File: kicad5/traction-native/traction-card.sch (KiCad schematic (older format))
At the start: 297 parts, among them Y1 CX3225GA40000D0PTVCC

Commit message: Rev A.16: round 17 — gap closure (F174-F189) + round 16 rev A.15 (F167-F173): every gap closed, upgraded or numbered
Round 16 (rev A.15, three rechecks of 32214be): exciter MFB gain 24 k -> 28 k with the amplitude
planes (setpoint 7.2 V pp at the monitor), unidirectional exciter TVS, /33X hold 0.07 A, firmware
acquisition contracts (phase triplets, resolver frame age, coherent SDADC frames); BOM furnished
(spec-class capacitors, drawn-size gate in bom-gen, last placeholders bound with archived sheets).

Round 17 (rev A.16, "close all gaps" / "feel free to upgrade"):
- Hardware: DEXP/DEXN PMEG4050EP-Q rated back-drive diversion (closes the ALM2402 OPEN row);
  exciter TVS -> SMDJ8.5A-HRA (3 kW, AEC-Q101, same pad); fault rows split single fault (PASS
  at any source impedance) vs load-dump-coincident double event; LV entry re-designed as
  LET-THROUGH for ISO 16750-2 test B (TPSMC33A-VR/TPSMC18A-VR anti-series pair at the pin ahead
  of the reverse Schottky, TPSMC33CA-VR on the power board, CLVC3 100 uF hybrid polymer, FLVC
  5 A fuse, DIGN US1M, ULDO15 D2PAK) — pulse 1 was avalanching DREVC, the 2023 26 V jump start
  opened the old TVS, the polyfuse was undersized at 9 V; RFS4 -> ESR18 1206.
- Stale/unsourced rows recomputed: cold-crank excitation, PTC hold (IR-13), discharge resistor
  no-flame statement, hall reference drift, ASC command-path collapse.
- KiCad: a KiCad 9/10 set (kicad/traction, Traction-Inverter-KiCad-modern.zip) proved by
  kicad-cli netlist export on every board with mutation tests; KiCad 10 cannot resolve the KiCad 5
  legacy symbols; the proof exposed harness pins numbered P1-P40 and the SMDJ drawn as a resistor
  in the legacy generator — fixed; sym-lib-table + cache library in both legacy sets.
- Firmware: all 35 open contract items closed (FW-08 zero-current decision, FW-31 liveness,
  FW-32 UDS service-lock routine, FW-33 supply-overvoltage supervision), FS26 watchdog answer
  3.0 ms -> 2.0 ms, ASC-exit release wait CAL, 39-row silicon/RM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
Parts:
- added RCPD1, RCPD2, RCPD3, RHWP: 10k, R0603, symbol traction-r1:R
- CAND1: renamed from CCLR; value 15nF -> 100nF; MPN MLCC-15nF-50V-C0G -> MLCC-CLASS
- CAND2: renamed from CFLTD; value 3.3nF -> 100nF; MPN MLCC-3.3nF-50V-C0G -> MLCC-CLASS
- CASCG: renamed from DFO; value BAT46ZFILM -> 100nF; footprint SOD123 -> C0603; symbol traction-r1:D -> traction-r1:C; LCSC C283255 -> CLASS; MPN BAT46ZFILM -> MLCC-100nF-16V
- CBAL: renamed from CBTP; value 22nF -> 1nF; MPN MLCC-CLASS -> MLCC-1nF-50V-C0G
- CBTC: renamed from CSB1; value 22uF -> 47nF; footprint C0805 -> C0603; MPN MLCC-CLASS -> MLCC-47nF-50V-X7R-0603
- CBTP: renamed from CSB2; value 22uF -> 22nF; footprint C0805 -> C0603; MPN MLCC-CLASS -> MLCC-22nF-50V-X7R-0603
- CCAN1: renamed from LCAN2; value ACT45B-101-2P-TL003 -> 1uF; footprint CMC1210 -> C0603; symbol traction-r1:ACT45B-101-2P-TL003 -> traction-r1:C; MPN ACT45B-101-2P-TL003 -> MLCC-1uF-25V
- CCAN2: renamed from JVEH; value TE 770669-1 (AMPSEAL 23) -> 1uF; footprint AMPSEAL23 -> C0603; symbol traction-r1:TE_770669-1__AMPSEAL_23_ -> traction-r1:C; MPN TE 770669-1 (AMPSEAL 23) -> MLCC-1uF-25V
- CCLR: renamed from CFLTF; value 100pF -> 15nF; MPN MLCC-100pF-16V -> MLCC-15nF-50V-C0G
- CCOSA1: renamed from CCOSF1; MPN MLCC-CLASS -> MLCC-22pF-50V-C0G-0603
- CCOSA2: renamed from CCOSF2; value 22pF -> 220pF; MPN MLCC-CLASS -> MLCC-220pF-50V-C0G-0603
- CCOSA3: renamed from RCOS1; value 12k -> 22pF; footprint R0603 -> C0603; symbol traction-r1:R -> traction-r1:C; MPN R0603-CLASS -> MLCC-22pF-50V-C0G-0603
- CCOSD: renamed from RCOS2; value 12k -> 47pF; footprint R0603 -> C0603; symbol traction-r1:R -> traction-r1:C; MPN R0603-CLASS -> MLCC-47pF-50V-C0G-0603
- CCOSF1: renamed from RCOSF1; value 12k -> 22pF; footprint R0603 -> C0603; symbol traction-r1:R -> traction-r1:C; MPN R0603-CLASS -> MLCC-22pF-50V-C0G-0603
- CCOSF2: renamed from RCOSF2; value 12k -> 22pF; footprint R0603 -> C0603; symbol traction-r1:R -> traction-r1:C; MPN R0603-CLASS -> MLCC-22pF-50V-C0G-0603
- CCT1: renamed from TVSC2; value PESD2IVN24-T -> 4.7nF; footprint SOT23 -> C0603; symbol traction-r1:PESD2IVN24-T -> traction-r1:C; LCSC C406047 -> CLASS; MPN PESD2IVN24-T -> MLCC-4.7nF-50V
- CCT2: renamed from FVS1; value MF-LSMF -> 4.7nF; footprint PTC1206 -> C0603; symbol traction-r1:F -> traction-r1:C; MPN MF-LSMF-CLASS -> MLCC-4.7nF-50V
- CEXA1: renamed from CEXA3; value 100nF -> 220pF; MPN MLCC-CLASS -> MLCC-220pF-50V-C0G-0603
- CEXA2: renamed from CEXA4; value 47pF -> 1.5nF; MPN MLCC-CLASS -> MLCC-1.5nF-50V-C0G-0603
- CEXA3: renamed from CEXD; value 4.7uF -> 100nF; MPN MLCC-CLASS -> MLCC-100nF-50V-X7R-0603
- CEXA4: renamed from CEXM; value 220pF -> 47pF; MPN MLCC-220pF-50V-C0G -> MLCC-47pF-50V-C0G-0603
- CEXD: renamed from CLDE; value 22uF -> 4.7uF; footprint C0603 -> C1206; MPN MLCC-CLASS -> MLCC-4.7uF-25V-X7R
- CEXM: renamed from CLDEC; value 270pF -> 220pF; MPN MLCC-CLASS -> MLCC-220pF-50V-C0G
- CFLTD: renamed from CFLTF2; value 100pF -> 3.3nF; MPN MLCC-100pF-16V -> MLCC-3.3nF-50V-C0G
- CFLTF: renamed from CLAT2; value 100nF -> 100pF; MPN MLCC-100nF-16V -> MLCC-100pF-16V
- CFLTF2: renamed from CSCH; value 100nF -> 100pF; MPN MLCC-100nF-16V -> MLCC-100pF-16V
- CIGN: renamed from DIGN; value 1N4148WS -> 100nF; footprint SOD323 -> C0603; symbol traction-r1:D -> traction-r1:C; LCSC C2128 -> CLASS; MPN 1N4148WS -> MLCC-100nF-50V
- CIGNS: renamed from RIGN1; value 5.1k -> 100nF; footprint R0603 -> C0603; symbol traction-r1:R -> traction-r1:C; MPN R0603-5k1 -> MLCC-CLASS
- CILK: renamed from RILK2; value 10k -> 2.2nF; footprint R0603 -> C0603; symbol traction-r1:R -> traction-r1:C; MPN R0603-10k -> MLCC-2.2nF-50V
- CLAT: renamed from RARB; value 10k -> 100nF; footprint R0603 -> C0603; symbol traction-r1:R -> traction-r1:C; MPN R0603-10k -> MLCC-100nF-16V
- CLDE: renamed from FEXN; value MF-MSMF020/33X -> 22uF; footprint 1812 -> C1210; symbol traction-r1:F -> traction-r1:C; MPN MF-MSMF020/33X -> MLCC-22uF-25V-X7R-1210
- CLDEC: renamed from FEXP; value MF-MSMF020/33X -> 270pF; footprint 1812 -> C0603; symbol traction-r1:F -> traction-r1:C; MPN MF-MSMF020/33X -> MLCC-270pF-50V-C0G-0603
- CLVC3: renamed from CLVSM; value 100nF -> 100uF; footprint C0603 -> CAP-ALU-SMD-G-10x10.2; symbol traction-r1:C -> traction-r1:CP; MPN MLCC-100nF-50V -> EEH-ZC1H101P
- CLVSM: renamed from DREVC; value STPS5L60S -> 100nF; footprint SMC -> C0603; symbol traction-r1:D -> traction-r1:C; LCSC C140620 -> CLASS; MPN STPS5L60S -> MLCC-100nF-50V
- CMD1, CMD10, CMD11, CMD12, CMD2, CMD3, CMD4, CMD5, CMD6, CMD7, CMD8, CMD9: footprint C0402 -> C0603; MPN MLCC-100nF-16V -> MLCC-100nF-16V-X7R-0603
- CMT1F: renamed from RMT1P; value 10k -> 47nF; footprint R0603 -> C0603; symbol traction-r1:R -> traction-r1:C; MPN R0603-CLASS -> MLCC-47nF-25V
- CMT2F: renamed from RMT1S; value 1k -> 47nF; footprint R0603 -> C0603; symbol traction-r1:R -> traction-r1:C; MPN R0603-CLASS -> MLCC-47nF-25V
- COF1: renamed from RVD1A; value 10k -> 100nF; footprint R0603 -> C0603; symbol traction-r1:R -> traction-r1:C; MPN R0603-10k-0.1% -> MLCC-CLASS
- COR1: renamed from CILK; value 2.2nF -> 100nF; MPN MLCC-2.2nF-50V -> MLCC-CLASS
- COR2: renamed from RILK1; value 10k -> 100nF; footprint R0603 -> C0603; symbol traction-r1:R -> traction-r1:C; MPN R0603-10k -> MLCC-CLASS
- CSB1: renamed from CSB3; MPN MLCC-CLASS -> MLCC-22uF-16V-X7R-0805
- CSB2: renamed from CSB3B; footprint C0603 -> C0805; MPN MLCC-CLASS -> MLCC-22uF-16V-X7R-0805
- CSB3: renamed from CSB4; value 10uF -> 22uF; MPN MLCC-CLASS -> MLCC-22uF-10V-X7R-0805
- CSB3B: renamed from CSB5; value 1uF -> 22uF; MPN MLCC-1uF-16V-X7R-0805 -> MLCC-22uF-10V-X7R-0805
- CSB4: renamed from CSB6; value 4.7uF -> 10uF; MPN MLCC-CLASS -> MLCC-10uF-10V-X7R-0805
- CSB5: renamed from CSB7; value 10uF -> 1uF; MPN MLCC-CLASS -> MLCC-1uF-16V-X7R-0805
- CSB6: renamed from CSB8; value 10uF -> 4.7uF; MPN MLCC-CLASS -> MLCC-4.7uF-10V-X7R-0805
- CSB7: renamed from CVBOS; value 4.7uF -> 10uF; footprint C0603 -> C0805; MPN MLCC-CLASS -> MLCC-10uF-16V-X7R-0805
- CSB8: renamed from CVDIG; value 1uF -> 10uF; footprint C0603 -> C0805; MPN MLCC-CLASS -> MLCC-10uF-16V-X7R-0805
- CSCH2: renamed from DCLR; value BAT46ZFILM -> 100nF; footprint SOD123 -> C0603; symbol traction-r1:D -> traction-r1:C; LCSC C283255 -> CLASS; MPN BAT46ZFILM -> MLCC-100nF-16V
- CSCH3: renamed from DFLT1; value BAT46ZFILM -> 100nF; footprint SOD123 -> C0603; symbol traction-r1:D -> traction-r1:C; LCSC C283255 -> CLASS; MPN BAT46ZFILM -> MLCC-100nF-16V
- CSINA1: renamed from CSINF1; MPN MLCC-CLASS -> MLCC-22pF-50V-C0G-0603
- CSINA2: renamed from CSINF2; value 22pF -> 220pF; MPN MLCC-CLASS -> MLCC-220pF-50V-C0G-0603
- CSINA3: renamed from RSIN1; value 12k -> 22pF; footprint R0603 -> C0603; symbol traction-r1:R -> traction-r1:C; MPN R0603-CLASS -> MLCC-22pF-50V-C0G-0603
- CSIND: renamed from RSIN2; value 12k -> 47pF; footprint R0603 -> C0603; symbol traction-r1:R -> traction-r1:C; MPN R0603-CLASS -> MLCC-47pF-50V-C0G-0603
- CSINF1: renamed from RSINF1; value 12k -> 22pF; footprint R0603 -> C0603; symbol traction-r1:R -> traction-r1:C; MPN R0603-CLASS -> MLCC-22pF-50V-C0G-0603
- CSINF2: renamed from RSINF2; value 12k -> 22pF; footprint R0603 -> C0603; symbol traction-r1:R -> traction-r1:C; MPN R0603-CLASS -> MLCC-22pF-50V-C0G-0603
- CSNUF: renamed from RSNVP; value 5.1k -> 47nF; footprint R0603 -> C0603; symbol traction-r1:R -> traction-r1:C; MPN R0603-5k1-1% -> MLCC-47nF-25V
- CSNVF: renamed from RSNWP; value 5.1k -> 47nF; footprint R0603 -> C0603; symbol traction-r1:R -> traction-r1:C; MPN R0603-5k1-1% -> MLCC-47nF-25V
- CSNWF: renamed from RTMR; value 0R -> 47nF; footprint R0603 -> C0603; symbol traction-r1:R -> traction-r1:C; MPN R0603-CLASS -> MLCC-47nF-25V
- CTAMBF: renamed from RTHS; value 10k -> 47nF; footprint R0603 -> C0603; symbol traction-r1:R -> traction-r1:C; MPN NTC-10k-0603 -> MLCC-47nF-25V
- CTHSF: renamed from RTHSP; value 10k -> 47nF; footprint R0603 -> C0603; symbol traction-r1:R -> traction-r1:C; MPN R0603-10k-1% -> MLCC-47nF-25V
- CUB1: renamed from LUB; value FB-220R-1A -> 3.3nF; footprint FB0805 -> C0603; symbol traction-r1:L -> traction-r1:C; MPN FB-220R-1A -> MLCC-3.3nF-50V
- CUB2: renamed from RUB0; value 100k -> 100nF; footprint R0603 -> C0603; symbol traction-r1:R -> traction-r1:C; MPN R0603-100k -> MLCC-100nF-25V
- CUS1: renamed from RUB1; value 100R -> 47nF; footprint R0603 -> C0603; symbol traction-r1:R -> traction-r1:C; MPN R0603-100R -> MLCC-47nF-25V
- CUS2: renamed from RUB2; value 100R -> 4.7nF; footprint R0603 -> C0603; symbol traction-r1:R -> traction-r1:C; MPN R0603-100R -> MLCC-4.7nF-50V
- CVB1: renamed from LVB; value FB-220R-1A -> 3.3nF; footprint FB0805 -> C0603; symbol traction-r1:L -> traction-r1:C; MPN FB-220R-1A -> MLCC-3.3nF-50V
- CVB2: renamed from RVB0; value 100k -> 100nF; footprint R0603 -> C0603; symbol traction-r1:R -> traction-r1:C; MPN R0603-100k -> MLCC-100nF-25V
- CVBOS: renamed from DBAT; value BAT46ZFILM -> 4.7uF; footprint SOD123 -> C0805; symbol traction-r1:D -> traction-r1:C; LCSC C283255 -> CLASS; MPN BAT46ZFILM -> MLCC-4.7uF-25V-X7R-0805
- CVD1: renamed from RVD1B; value 10k -> 100pF; footprint R0603 -> C0603; symbol traction-r1:R -> traction-r1:C; MPN R0603-10k-0.1% -> MLCC-100pF-50V-C0G-0603
- CVD2: renamed from RVD2D; value 10k -> 100pF; footprint R0603 -> C0603; symbol traction-r1:R -> traction-r1:C; MPN R0603-10k-0.1% -> MLCC-100pF-50V-C0G-0603
- CVDIG: renamed from LCOR; value XAL4020-222MEC -> 1uF; footprint XAL4020 -> C0603; symbol traction-r1:L -> traction-r1:C; MPN XAL4020-222MEC -> MLCC-1uF-10V-X7R-0603
- CVM1: renamed from RVM1; value 24k -> 220nF; footprint R0603 -> C0603; symbol traction-r1:R -> traction-r1:C; MPN R0603-24k-1% -> MLCC-220nF-16V-X7R-0603
- CVM2: renamed from RVM2; value 24k -> 220nF; footprint R0603 -> C0603; symbol traction-r1:R -> traction-r1:C; MPN R0603-24k-1% -> MLCC-220nF-16V-X7R-0603
- CVS1: renamed from RVB1; value 100R -> 47nF; footprint R0603 -> C0603; symbol traction-r1:R -> traction-r1:C; MPN R0603-100R -> MLCC-47nF-25V
- CVS2: renamed from RVB2; value 100R -> 4.7nF; footprint R0603 -> C0603; symbol traction-r1:R -> traction-r1:C; MPN R0603-100R -> MLCC-4.7nF-50V
- CWB1: renamed from LWB; value FB-220R-1A -> 3.3nF; footprint FB0805 -> C0603; symbol traction-r1:L -> traction-r1:C; MPN FB-220R-1A -> MLCC-3.3nF-50V
- CWB2: renamed from RWB0; value 100k -> 100nF; footprint R0603 -> C0603; symbol traction-r1:R -> traction-r1:C; MPN R0603-100k -> MLCC-100nF-25V
- CWS1: renamed from RWB1; value 100R -> 47nF; footprint R0603 -> C0603; symbol traction-r1:R -> traction-r1:C; MPN R0603-100R -> MLCC-47nF-25V
- CWS2: renamed from RWB2; value 100R -> 4.7nF; footprint R0603 -> C0603; symbol traction-r1:R -> traction-r1:C; MPN R0603-100R -> MLCC-4.7nF-50V
- DBAT: renamed from LSBC; value XAL4040-103MEC -> BAT46ZFILM; footprint XAL4040 -> SOD123; symbol traction-r1:L -> traction-r1:D; LCSC CLASS -> C283255; MPN XAL4040-103MEC -> BAT46ZFILM
- DCOSP: renamed from CCOSD; value 47pF -> PESD2IVN24-T; footprint C0603 -> SOT23; symbol traction-r1:C -> traction-r1:PESD2IVN24-T; LCSC CLASS -> C406047; MPN MLCC-CLASS -> PESD2IVN24-T
- DEXN: renamed from REXA1; value 3k -> PMEG4050EP-Q; footprint R0603 -> SOD128; symbol traction-r1:R -> traction-r1:D; MPN R0603-CLASS -> PMEG4050EP-Q
- DEXP: renamed from REXA2; value 10k -> PMEG4050EP-Q; footprint R0603 -> SOD128; symbol traction-r1:R -> traction-r1:D; MPN R0603-CLASS -> PMEG4050EP-Q
- DFLT1: renamed from RDRB; value 10k -> BAT46ZFILM; footprint R0603 -> SOD123; symbol traction-r1:R -> traction-r1:D; LCSC CLASS -> C283255; MPN R0603-10k -> BAT46ZFILM
- DFLT2: renamed from RENP1; value 5.1k -> BAT46ZFILM; footprint R0603 -> SOD123; symbol traction-r1:R -> traction-r1:D; LCSC CLASS -> C283255; MPN R0603-5k1 -> BAT46ZFILM
- DFO: renamed from RASCP; value 10k -> BAT46ZFILM; footprint R0603 -> SOD123; symbol traction-r1:R -> traction-r1:D; LCSC CLASS -> C283255; MPN R0603-10k -> BAT46ZFILM
- DIGN: renamed from RIGN2; value 10k -> US1M; footprint R0603 -> SMA; symbol traction-r1:R -> traction-r1:D; LCSC CLASS -> C412437; MPN R0603-10k -> US1M
- DREVC: renamed from DTVSC; value TPSMC24CA-VR -> STPS5L60S; LCSC C1975284 -> C140620; MPN TPSMC24CA-VR -> STPS5L60S
- DSINP: renamed from CSIND; value 47pF -> PESD2IVN24-T; footprint C0603 -> SOT23; symbol traction-r1:C -> traction-r1:PESD2IVN24-T; LCSC CLASS -> C406047; MPN MLCC-CLASS -> PESD2IVN24-T
- DTVSC: renamed from FLVC; value MF-LSMF300/24X-2 -> TPSMC33A-VR; footprint PTC2920 -> SMC; symbol traction-r1:F -> traction-r1:D; LCSC C719172 -> CLASS; MPN MF-LSMF300/24X-2 -> TPSMC33A-VR
- DTVSC2: renamed from FVBH; value MF-LSMF300/24X-2 -> TPSMC18A-VR; footprint PTC2920 -> SMC; symbol traction-r1:F -> traction-r1:D; LCSC C719172 -> CLASS; MPN MF-LSMF300/24X-2 -> TPSMC18A-VR
- FEXN: renamed from REXA3; value 10k -> MF-MSMF020/33X; footprint R0603 -> 1812; symbol traction-r1:R -> traction-r1:F; MPN R0603-CLASS -> MF-MSMF020/33X
- FEXP: renamed from REXA4; value 24k -> MF-MSMF020/33X; footprint R0603 -> 1812; symbol traction-r1:R -> traction-r1:F; MPN R0603-CLASS -> MF-MSMF020/33X
- FLVC: renamed from FVBL; value MF-LSMF300/24X-2 -> 0680L5000-05; footprint PTC2920 -> 2410; LCSC C719172 -> CLASS; MPN MF-LSMF300/24X-2 -> 0680L5000-05
- FMT1: renamed from RMT2P; value 10k -> 0438.375WRA; footprint R0603 -> F0603; symbol traction-r1:R -> traction-r1:F; MPN R0603-CLASS -> 0438.375WRA
- FMT2: renamed from RMT2S; value 1k -> 0438.375WRA; footprint R0603 -> F0603; symbol traction-r1:R -> traction-r1:F; MPN R0603-CLASS -> 0438.375WRA
- FVBH: renamed from LFC; value FB-120R-3A -> MF-LSMF300/24X-2; footprint FB1206 -> PTC2920; symbol traction-r1:L -> traction-r1:F; LCSC CLASS -> C719172; MPN FB-120R-3A -> MF-LSMF300/24X-2
- FVBL: renamed from RLVSD; value 4.7k -> MF-LSMF300/24X-2; footprint R0603 -> PTC2920; symbol traction-r1:R -> traction-r1:F; LCSC CLASS -> C719172; MPN R0603-4k7 -> MF-LSMF300/24X-2
- FVS1: renamed from LVS4; value FB-470R -> MF-MSMF010/60X; footprint FB0603 -> PTC1812; symbol traction-r1:L -> traction-r1:F; MPN FB-470R-CLASS -> MF-MSMF010/60X
- JICC: renamed from RCPD3; value 10k -> IPL1-120-01-L-D-K; footprint R0603 -> HDR2x20-2.54; symbol traction-r1:R -> traction-r1:IPL1-120-01-L-D-K; MPN R0603-10k -> IPL1-120-01-L-D-K
- JLEM: renamed from UUB1; value OPA376AQDBVRQ1 -> T2M-105-01-L-D-TH-WT; footprint SOT23-5 -> HDR2x5; symbol traction-r1:OPA376AQDBVRQ1 -> traction-r1:T2M-105-01-L-D-TH-WT; MPN OPA376AQDBVRQ1 -> T2M-105-01-L-D-TH-WT
- JVEH: renamed from LVS3; value FB-470R -> TE 770669-1 (AMPSEAL 23); footprint FB0603 -> AMPSEAL23; symbol traction-r1:L -> traction-r1:TE_770669-1__AMPSEAL_23_; MPN FB-470R-CLASS -> TE 770669-1 (AMPSEAL 23)
- LCAN1: renamed from CCT1; value 4.7nF -> ACT45B-101-2P-TL003; footprint C0603 -> CMC1210; symbol traction-r1:C -> traction-r1:ACT45B-101-2P-TL003; MPN MLCC-4.7nF-50V -> ACT45B-101-2P-TL003
- LCAN2: renamed from CCT2; value 4.7nF -> ACT45B-101-2P-TL003; footprint C0603 -> CMC1210; symbol traction-r1:C -> traction-r1:ACT45B-101-2P-TL003; MPN MLCC-4.7nF-50V -> ACT45B-101-2P-TL003
- LCOR: renamed from RAGT; value 0R -> XAL4020-222MEC; footprint R0603 -> XAL4020; symbol traction-r1:R -> traction-r1:L; MPN R0603-CLASS -> XAL4020-222MEC
- LFC: renamed from RLVSG; value 10k -> BLM31PG121SH1L; footprint R0603 -> FB1206; symbol traction-r1:R -> traction-r1:L; MPN R0603-10k -> BLM31PG121SH1L
- LSBC: renamed from RDBG; value 10k -> XAL4040-103MEC; footprint R0603 -> XAL4040; symbol traction-r1:R -> traction-r1:L; MPN R0603-CLASS -> XAL4040-103MEC
- LUB: renamed from RUB3; value 100R -> BLM21PG221SH1D; footprint R0603 -> FB0805; symbol traction-r1:R -> traction-r1:L; MPN R0603-100R -> BLM21PG221SH1D
- LVB: renamed from RVB3; value 100R -> BLM21PG221SH1D; footprint R0603 -> FB0805; symbol traction-r1:R -> traction-r1:L; MPN R0603-100R -> BLM21PG221SH1D
- LVS1: renamed from JICC; value IPL1-120-01-L-D-K -> MMZ1608B471CTDH5; footprint HDR2x20-2.54 -> FB0603; symbol traction-r1:IPL1-120-01-L-D-K -> traction-r1:L; MPN IPL1-120-01-L-D-K -> MMZ1608B471CTDH5
- LVS2: renamed from RCPD0; value 10k -> MMZ1608B471CTDH5; footprint R0603 -> FB0603; symbol traction-r1:R -> traction-r1:L; MPN R0603-10k -> MMZ1608B471CTDH5
- LVS3: renamed from RCPD1; value 10k -> MMZ1608B471CTDH5; footprint R0603 -> FB0603; symbol traction-r1:R -> traction-r1:L; MPN R0603-10k -> MMZ1608B471CTDH5
- LVS4: renamed from RCPD2; value 10k -> MMZ1608B471CTDH5; footprint R0603 -> FB0603; symbol traction-r1:R -> traction-r1:L; MPN R0603-10k -> MMZ1608B471CTDH5
- LWB: renamed from RWB3; value 100R -> BLM21PG221SH1D; footprint R0603 -> FB0805; symbol traction-r1:R -> traction-r1:L; MPN R0603-100R -> BLM21PG221SH1D
- QBAL: renamed from CBAL; value 1nF -> SQ2310ES; footprint C0603 -> SOT23; symbol traction-r1:C -> traction-r1:SQ2310ES; MPN MLCC-1nF-50V-C0G -> SQ2310ES
- RAGT: renamed from RSB1; value 52.3k -> 0R; footprint R0603 -> R0805; MPN R0603-CLASS -> R0805-0R-CLASS
- RARB: renamed from RFS1; value 1k -> 10k; MPN R0603-1k -> R0603-10k
- RCOS1: renamed from RCOSR1; value 120R -> 12k; MPN R0603-120R -> R0603-CLASS
- RCOS2: renamed from RCOSR2; value 120R -> 12k; MPN R0603-120R -> R0603-CLASS
- RCOSF1: renamed from JLEM; value T2M-105-01-L-D-TH-WT -> 12k; footprint HDR2x5 -> R0603; symbol traction-r1:T2M-105-01-L-D-TH-WT -> traction-r1:R; MPN T2M-105-01-L-D-TH-WT -> R0603-CLASS
- RCOSF2: renamed from USNSU; value HC5FW900-S -> 12k; footprint OffBoard -> R0603; symbol traction-r1:HC5FW900-S -> traction-r1:R; MPN HC5FW900-S -> R0603-CLASS
- RCOSR1: renamed from USNSV; value HC5FW900-S -> 120R; footprint OffBoard -> R0603; symbol traction-r1:HC5FW900-S -> traction-r1:R; MPN HC5FW900-S -> R0603-120R
- RCOSR2: renamed from USNSW; value HC5FW900-S -> 120R; footprint OffBoard -> R0603; symbol traction-r1:HC5FW900-S -> traction-r1:R; MPN HC5FW900-S -> R0603-120R
- RCPD0: renamed from RHWP; MPN R0603-10k-1% -> R0603-10k
- RCT1A: renamed from UCAN2; value TCAN1042HGVDRQ1 -> 60.4R; footprint SOIC8 -> R0603; symbol traction-r1:TCAN1042HGVDRQ1 -> traction-r1:R; LCSC C132550 -> CLASS; MPN TCAN1042HGVDRQ1 -> R0603-60R4-1%
- RCT1B: renamed from CCAN2; value 1uF -> 60.4R; footprint C0603 -> R0603; symbol traction-r1:C -> traction-r1:R; MPN MLCC-1uF-25V -> R0603-60R4-1%
- RCT2A: renamed from LVS1; value FB-470R -> 60.4R; footprint FB0603 -> R0603; symbol traction-r1:L -> traction-r1:R; MPN FB-470R-CLASS -> R0603-60R4-1%
- RCT2B: renamed from LVS2; value FB-470R -> 60.4R; footprint FB0603 -> R0603; symbol traction-r1:L -> traction-r1:R; MPN FB-470R-CLASS -> R0603-60R4-1%
- RDRB: renamed from RFCB; value 100k -> 10k; MPN R0603-100k -> R0603-10k
- RENP1: renamed from RFLTC; value 10k -> 5.1k; MPN R0603-10k -> R0603-5k1
- REXA1: renamed from REXB1; value 24k -> 3k
- REXA2: renamed from REXB2; value 24k -> 10k
- REXA3: renamed from REXB3; value 24k -> 10k
- REXA4: renamed from REXB4; value 24k -> 28k
- REXB1: renamed from REXM1; value 18k -> 24k; MPN R0603-18k-1% -> R0603-CLASS
- REXB2: renamed from REXM2; value 42.2k -> 24k; MPN R0603-42k2-1% -> R0603-CLASS
- REXB3: renamed from REXM3; value 18k -> 24k; MPN R0603-18k-1% -> R0603-CLASS
- REXB4: renamed from REXM4; value 84.5k -> 24k; MPN R0603-84k5-1% -> R0603-CLASS
- REXM1: renamed from RLDE1; value 38.3k -> 18k; MPN R0603-CLASS -> R0603-18k-1%
- REXM2: renamed from RLDE2; value 10k -> 42.2k; MPN R0603-CLASS -> R0603-42k2-1%
- REXM3: renamed from RSDN; value 10k -> 18k; MPN R0603-CLASS -> R0603-18k-1%
- REXM4: renamed from RSXN; value 2.2R -> 84.5k; footprint R1206 -> R0603; MPN R1206-2R2-1% -> R0603-84k5-1%
- RFCB: renamed from RFLTD; value 10k -> 100k; MPN R0603-10k -> R0603-100k
- RFLTC: renamed from RFLTP1; value 5.1k -> 10k; MPN R0603-5k1 -> R0603-10k
- RFLTD: renamed from RFLTP2; value 5.1k -> 10k; MPN R0603-5k1 -> R0603-10k
- RFLTP1: renamed from RGPD; value 10k -> 5.1k; MPN R0603-10k -> R0603-5k1
- RFLTP2: renamed from RLAT2; value 10k -> 5.1k; MPN R0603-10k -> R0603-5k1
- RFS2: renamed from RFS4; value 1k -> 10k; MPN ESR03EZPF1001 -> R0603-10k
- RFS3: renamed from RLAT1; value 10k -> 1k; MPN R0603-10k -> R0603-1k
- RFS4: renamed from ZSET; value BZT52-B5V6 -> 1k; footprint SOD123 -> R1206; symbol traction-r1:D -> traction-r1:R; MPN BZT52-B5V6 -> ESR18EZPF1001
- RIGN1: renamed from RIGNS1; value 47k -> 5.1k; MPN R0603-CLASS -> R0603-5k1
- RIGN2: renamed from RIGNS2; MPN R0603-CLASS -> R0603-10k
- RIGNS1: renamed from UAND1; value 74LVC1G11GW-Q100 -> 47k; footprint SOT363 -> R0603; symbol traction-r1:74LVC1G11GW-Q100 -> traction-r1:R; LCSC C548242 -> CLASS; MPN 74LVC1G11GW-Q100 -> R0603-CLASS
- RIGNS2: renamed from UAND2; value 74LVC1G11GW-Q100 -> 10k; footprint SOT363 -> R0603; symbol traction-r1:74LVC1G11GW-Q100 -> traction-r1:R; LCSC C548242 -> CLASS; MPN 74LVC1G11GW-Q100 -> R0603-CLASS
- RILK3: renamed from UVMB1; value OPA348AQDBVRQ1 -> 10k; footprint SOT23-5 -> R0603; symbol traction-r1:OPA348AQDBVRQ1 -> traction-r1:R; LCSC C2877787 -> CLASS; MPN OPA348AQDBVRQ1 -> R0603-10k
- RILK4: renamed from UVMB2; value OPA348AQDBVRQ1 -> 10k; footprint SOT23-5 -> R0603; symbol traction-r1:OPA348AQDBVRQ1 -> traction-r1:R; LCSC C2877787 -> CLASS; MPN OPA348AQDBVRQ1 -> R0603-10k
- RLAT1: renamed from UOR1; value 74LVC1G32GW-Q100 -> 10k; footprint SOT353 -> R0603; symbol traction-r1:74LVC1G32GW-Q100 -> traction-r1:R; LCSC C548334 -> CLASS; MPN 74LVC1G32GW-Q100 -> R0603-10k
- RLAT2: renamed from RRDB; value 100k -> 10k; MPN R0603-100k -> R0603-10k
- renumbered CSCH2 to CLAT2, CSCH3 to CSCH, DFLT2 to DCLR, RFS2 to RASCP, RSB2 to RDBG, RFS3 to RFS1, RQDM to RGPD, RILK3 to RILK1, RILK4 to RILK2, RVD2A to RVD1C, RVD2B to RVD1D, RVM3 to RVM1, RVM4 to RVM2, USCH3 to USCH
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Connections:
- net AGND: now also CCOSA1.2, CCOSA3.2, CEXA4.2, CIGNS.2, CLDE.2, CMT1F.2, CMT2F.2, COF1.2, CSINA1.2, CSINA3.2, CSNUF.2, CSNVF.2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; no longer CCAN2.10 (MT1R), CCAN2.12 (MT2R), CEXA3.2, JLEM.2, LCOR.1, LVS1.3 (P3_AGND), RCOSF1.10 (G3), RCOSF1.3 (G1), RCOSF1.6 (G2), RCOSF1.9 (SH), RCOSF2.3, RCOSF2.5 (E1)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
- net AMUXO: now also RSB3.1, USBC.29 (AMUX); no longer RSB1.1, ZLVS.29 (AMUX)
- net ASC_CLR_M: now also RFS3.1; no longer RFS1.1
- net ASC_CLR_N: now also RLAT1.2, ULAT.6 (CLR_N); no longer RFS1.2, RV5GS.6 (CLR_N)
- net ASC_CMD: now also JICC.15 (P15_ASC_CMD), RARB.1, UASCG.4 (Y); no longer CLAT.1, LVS1.15 (P15_ASC_CMD), RV5GP.4 (Y)
- net ASC_CMD_RB: now also RARB.2; no longer CLAT.2
- net ASC_Q: now also RASCP.1, UASCG.2 (A), ULAT.5 (Q); no longer DFO.1, RV5GP.2 (A), RV5GS.5 (Q)
- net ASC_REQ: now also ULAT.1 (CLK), RCPD1.1; no longer LVS3.1, RV5GS.1 (CLK)
- net ASC_SET_B: now also ULAT.7 (PRE_N), USCH2.5 (Y2); no longer RV5GS.7 (PRE_N), ULAT2.5 (Y2)
- net ASC_SET_N: now also RFS1.2, RFS2.2, USCH2.3 (A2), ZSET.2; no longer RARB.2, RASCP.2, RFS4.2, ULAT2.3 (A2)
- net BATSNS: now also DBAT.2, USBC.48 (BATSENSE); no longer CVBOS.2, ZLVS.48 (BATSENSE)
- net BCTRL: now also CBAL.1; no longer RLVSM.1 (G)
- net CAN0_RX: now also UCAN1.4 (RXD); no longer TVSM1.4 (RXD)
- net CAN0_TX: now also UCAN1.1 (TXD); no longer TVSM1.1 (TXD)
- net CAN1_RX: now also UCAN2.4 (RXD); no longer RCT1A.4 (RXD)
- net CAN1_TX: now also UCAN2.1 (TXD); no longer RCT1A.1 (TXD)
- net CANH1: now also LCAN1.4 (A2), LVS1.2, TVSC1.1 (A); no longer RCT2A.2, RMT2P.4 (A2), RMT2S.1 (A)
- net CANH1_T: now also LCAN1.1 (A1), RCT1A.1, UCAN1.7 (CANH); no longer RMT2P.1 (A1), TVSC1.1, TVSM1.7 (CANH)
- net CANH2: now also LCAN2.4 (A2), LVS3.2, TVSC2.1 (A); no longer CCAN1.4 (A2), CCT1.1 (A), JVEH.2
- net CANH2_T: now also LCAN2.1 (A1), RCT2A.1, UCAN2.7 (CANH); no longer CCAN1.1 (A1), RCT1A.7 (CANH), TVSC2.1
- net CANL1: now also LCAN1.3 (B2), LVS2.2, TVSC1.2 (B); no longer RCT2B.2, RMT2P.3 (B2), RMT2S.2 (B)
- net CANL1_T: now also LCAN1.2 (B1), RCT1B.2, UCAN1.6 (CANL); no longer RMT2P.2 (B1), TVSM1.6 (CANL), UCAN1.2
- net CANL2: now also LCAN2.3 (B2), LVS4.2, TVSC2.2 (B); no longer CCAN1.3 (B2), CCT1.2 (B), FVS1.2
- net CANL2_T: now also LCAN2.2 (B1), RCT2B.2, UCAN2.6 (CANL); no longer CCAN1.2 (B1), RCT1A.6 (CANL), UCAN2.2
- net CANS1: now also CCT1.1, RCT1A.2, RCT1B.1; no longer LCAN1.1, TVSC1.2, UCAN1.1
- net CANS2: now also CCT2.1, RCT2A.2, RCT2B.1; no longer LCAN2.1, TVSC2.2, UCAN2.1
- net CORBT: now also CBTC.1, USBC.33 (CORE_BT); no longer USBC.1, ZLVS.33 (CORE_BT)
- net COSF_N: now also CCOSD.2, CCOSF2.1, RCOSF2.2, RCOSR2.1; no longer CCOSA2.1, CCOSF2.2, RCOS2.1, RSINF1.2 (B)
- net COSF_P: now also CCOSD.1, CCOSF1.1, RCOSF1.2, RCOSR1.1; no longer CCOSA1.1, CCOSF1.2, RCOS1.1, RSINF1.1 (A)
- net COS_N: now also CCOSA2.2, CCOSA3.1, RCOSR2.2; no longer RCOS2.2, RSINR1.2, RSINR2.1
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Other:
- note added: "rev A.16 - 26 sections - 301 components"
- note removed: "rev A.14 - 26 sections - 297 components"
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
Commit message: Rev A.17: round 18 — three rechecks of 4425af9 (F190-F198): diversion diodes on the amplifier node (loop passes RSX), diode cell cathode = pin 1 on all 35 diodes, exciter TVS/PTC rows at worst corners + ECU-asleep sustained short (WARN rows, layout rule, QP-RX-04 2b gate), anti-surge RSX, NCV4276C reverse current = QP-RX-05 gate + VR-33, IR-16/IR-42, firmware FW-34..36 (sample freshness, cadence-locked resolver frames, latency sign) + three self-found instances
Co-Authored-By: Claude Fable 5.1 <noreply@anthropic.com>
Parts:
- DBAT, DCLR, DEXN, DEXP, DFLT1, DFLT2, DFO, DIGN, DREVC, DTVSC, DTVSC2, ZLVS, ZSET: symbol traction-r1:D -> traction-r1:D_21
- RSXN, RSXP: MPN ERJ-8ENF2R20V -> ESR18EZPF2R20
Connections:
- net ASC_SET_N: now also ZSET.1; no longer ZSET.2
- net BATSNS: now also DBAT.1; no longer DBAT.2
- net DGND: now also DTVSC2.1, ZSET.2; no longer DTVSC2.2, ZSET.1
- net FAULT_OUT: now also DFO.2; no longer DFO.1
- net FCO: now also DREVC.2, DTVSC.1; no longer DREVC.1, DTVSC.2
- net FLT_CLR_N: now also DCLR.2; no longer DCLR.1
- net FLT_CMB_N: now also DFLT1.2, DFLT2.2; no longer DFLT1.1, DFLT2.1
- net FLT_HS_N: now also DFLT1.1; no longer DFLT1.2
- net FLT_LS_N: now also DFLT2.1; no longer DFLT2.2
- net FOUT_K: now also DFO.1; no longer DFO.2
- net IGN_D: now also DIGN.1; no longer DIGN.2
- net KL15: now also DIGN.2; no longer DIGN.1
- net LVS_G: now also ZLVS.2; no longer ZLVS.1
- net NRC: now also DREVC.1, ZLVS.1; no longer DREVC.2, ZLVS.2
- net TVSM: now also DTVSC.2, DTVSC2.2; no longer DTVSC.1, DTVSC2.1
- net V5A: now also DCLR.1; no longer DCLR.2
- net VBATC: now also DBAT.2; no longer DBAT.1
- net VEXD: now also DEXN.1, DEXP.1; no longer DEXN.2, DEXP.2
- net VREX_N: now also DEXN.2
- net VREX_NX: no longer DEXN.1
- net VREX_P: now also DEXP.2
- net VREX_PX: no longer DEXP.1
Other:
- note added: "rev A.17 - 26 sections - 301 components"
- note removed: "rev A.16 - 26 sections - 301 components"
- moved on the sheet: CEXA1, CEXA2, CEXA3, CEXA4, FEXN, FEXP, REXA1, REXA2, REXA3, REXA4, RSXN, RSXP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

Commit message: Rev A.18: round 19 — three rechecks of e315bf1 (F199-F204): PTC-current row at every permitted voltage (IR-16 0.08/0.14/0.37/0.26 Ω), ≥8 A TVS energy an explicit assumption + QP-RX-04 release criterion, window criterion fixed, exciter TVS → SMDJ7.0A-HRA (coupled island holds the 7.0 V class at a parked 12 V battery / the Marine rail), shared exciter-fault model run for the Marine port (QP-MA-11, kit-loom rule), FW-35 rewritten on an SWG-anchored time origin with clock-derived resync and bounded restart
Co-Authored-By: Claude Fable 5.1 <noreply@anthropic.com>
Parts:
- TVSEN, TVSEP: value SMDJ8.5A-HRA -> SMDJ7.0A-HRA; MPN SMDJ8.5A-HRA -> SMDJ7.0A-HRA
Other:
- note added: "rev A.18 - 26 sections - 301 components"
- note removed: "rev A.17 - 26 sections - 301 components"
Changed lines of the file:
@@
 Title "Traction Inverter — Control Card (S32K396 + FS26, ASIL D)"
 Date "2026-09-23"
-Rev "A.17"
+Rev "A.18"
 Comp "Traction Inverter 220 kW pk - Control card (LV), sheet 4 of 4"
 Comment1 "Inverter = Power board + Cap bank busbar + bolt-on Discharge board (all HV) + Control card (LV); safe state holds with any link lost"
@@
 VEHICLE-IF   -   1 section
 Text Notes 33460 22550 0    60   ~ 0
-rev A.17   -   26 sections   -   301 components
+rev A.18   -   26 sections   -   301 components
 Wire Notes Line
 	33400 23500 37850 23500
@@
 P 33450 7000
 F 0 "TVSEN" H 33450 6840 50  0000 C CNN
-F 1 "SMDJ8.5A-HRA" H 33450 7170 50  0000 C CNN
+F 1 "SMDJ7.0A-HRA" H 33450 7170 50  0000 C CNN
 F 2 "SMC" H 33450 7000 50  0001 C CNN
 F 3 "~" H 33450 7000 50  0001 C CNN
 F 4 "CLASS" H 33450 7000 50  0001 C CNN "LCSC"
-F 5 "SMDJ8.5A-HRA" H 33450 7000 50  0001 C CNN "MPN"
+F 5 "SMDJ7.0A-HRA" H 33450 7000 50  0001 C CNN "MPN"
 	1    33450 7000
 	1    0    0    -1
@@
 P 33450 5800
 F 0 "TVSEP" H 33450 5640 50  0000 C CNN
-F 1 "SMDJ8.5A-HRA" H 33450 5970 50  0000 C CNN
+F 1 "SMDJ7.0A-HRA" H 33450 5970 50  0000 C CNN
 F 2 "SMC" H 33450 5800 50  0001 C CNN
 F 3 "~" H 33450 5800 50  0001 C CNN
 F 4 "CLASS" H 33450 5800 50  0001 C CNN "LCSC"
-F 5 "SMDJ8.5A-HRA" H 33450 5800 50  0001 C CNN "MPN"
+F 5 "SMDJ7.0A-HRA" H 33450 5800 50  0001 C CNN "MPN"
 	1    33450 5800
 	1    0    0    -1

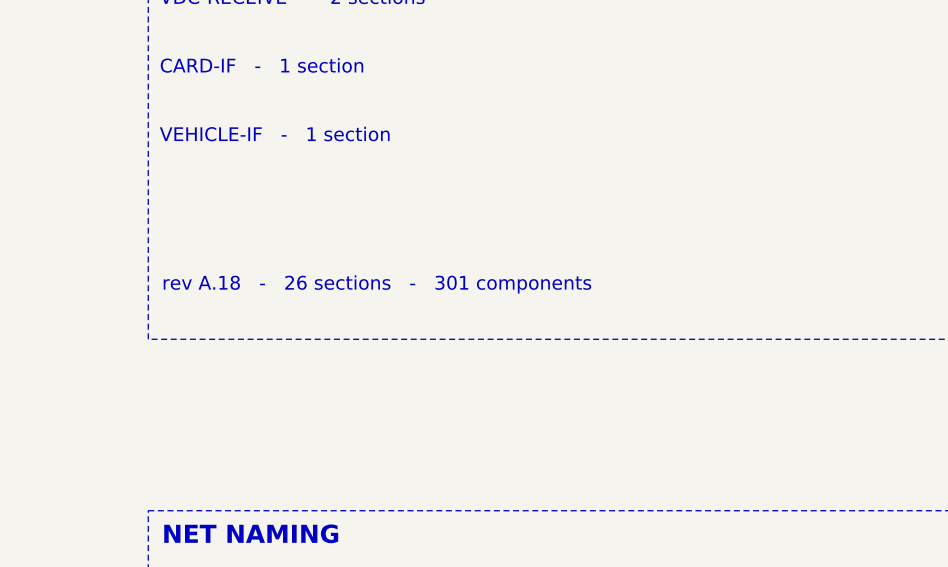
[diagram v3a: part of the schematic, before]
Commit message: Rev A.19: round 20 — three rechecks of 00f6252 (F205-F207): TVS alternate to the 7.0 V class + lock, 4XX discharge alternate 470→220 Ω + lock, T-05/T-06 firmware ID, 8.5 V-era figures re-derived at the IR-16 allocations
Co-Authored-By: Claude Fable 5.1 <noreply@anthropic.com>
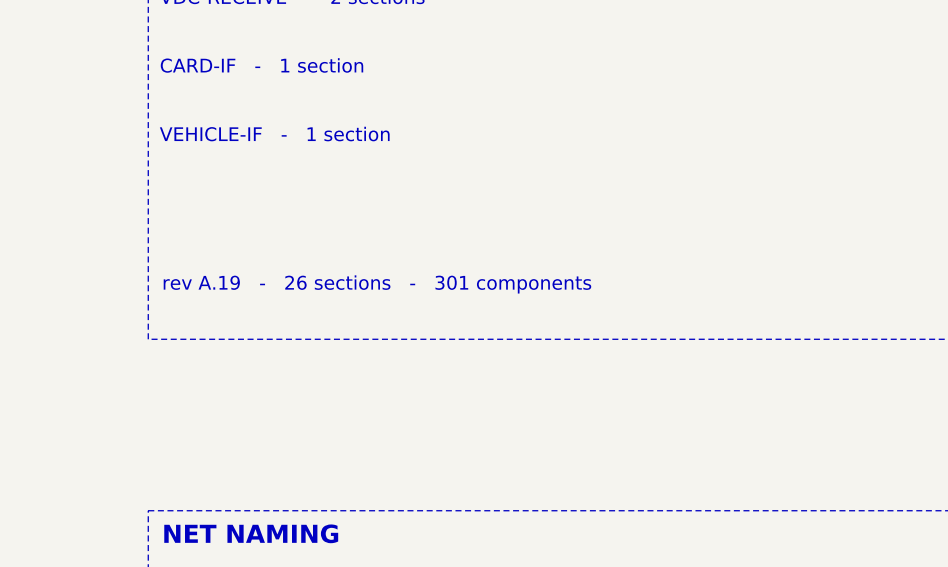
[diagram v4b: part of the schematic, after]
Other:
- note added: "rev A.19 - 26 sections - 301 components"
- note removed: "rev A.18 - 26 sections - 301 components"
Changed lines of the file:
@@
 Title "Traction Inverter — Control Card (S32K396 + FS26, ASIL D)"
 Date "2026-09-23"
-Rev "A.18"
+Rev "A.19"
 Comp "Traction Inverter 220 kW pk - Control card (LV), sheet 4 of 4"
 Comment1 "Inverter = Power board + Cap bank busbar + bolt-on Discharge board (all HV) + Control card (LV); safe state holds with any link lost"
@@
 VEHICLE-IF   -   1 section
 Text Notes 33460 22550 0    60   ~ 0
-rev A.18   -   26 sections   -   301 components
+rev A.19   -   26 sections   -   301 components
 Wire Notes Line
 	33400 23500 37850 23500

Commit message: Rev A.20: round 21 — three rechecks of 551c405 (F208): stale 0.29 Ω in gate ㉘ and the QP-RX-04 fixture instruction → 0.37 Ω, last 8.5 V-era figures aligned, Marine sweep cross-references at the current values
Co-Authored-By: Claude Fable 5.1 <noreply@anthropic.com>
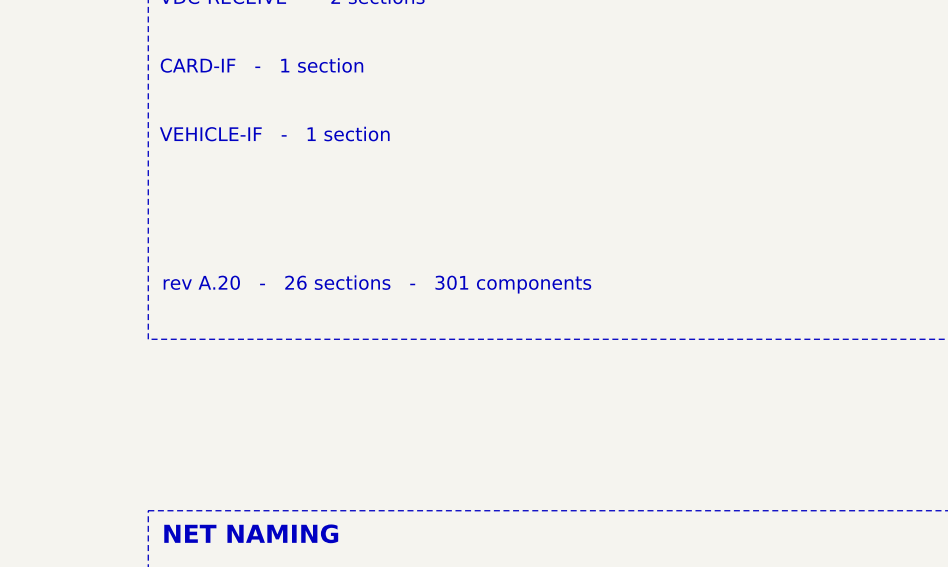
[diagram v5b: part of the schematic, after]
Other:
- note added: "rev A.20 - 26 sections - 301 components"
- note removed: "rev A.19 - 26 sections - 301 components"
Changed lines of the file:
@@
 Title "Traction Inverter — Control Card (S32K396 + FS26, ASIL D)"
 Date "2026-09-23"
-Rev "A.19"
+Rev "A.20"
 Comp "Traction Inverter 220 kW pk - Control card (LV), sheet 4 of 4"
 Comment1 "Inverter = Power board + Cap bank busbar + bolt-on Discharge board (all HV) + Control card (LV); safe state holds with any link lost"
@@
 VEHICLE-IF   -   1 section
 Text Notes 33460 22550 0    60   ~ 0
-rev A.19   -   26 sections   -   301 components
+rev A.20   -   26 sections   -   301 components
 Wire Notes Line
 	33400 23500 37850 23500

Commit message: Rev A.21: round 22 — three rechecks of 0ff44d9 (F209) + the layout handoff (F210–F213): every KiCad symbol bound to a footprint in a shipped traction.pretty (45 verbatim KiCad-10 patterns + 18 datasheet-drawn), fp-lib-table and per-board projects in all sets, pad-per-pin KiCad proof; NCV4276C 5-lead lands, ALM2402/TPS55340 thermal-pad pins, 2-pad crystal; QP §0.2 baseline and stale IDs; docs/layout-handoff.md
Co-Authored-By: Claude Fable 5.1 <noreply@anthropic.com>
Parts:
- CAND1, CAND2, CASCG, CBAL, CBTC, CBTP, CCAN1, CCAN2, CCLR, CCOSA1, CCOSA2, CCOSA3, CCOSD, CCOSF1, CCOSF2, CCT1, CCT2, CEXA1, CEXA2, CEXA3, CEXA4, CEXM, CFLTD, CFLTF, CFLTF2, CIGN, CIGNS, CILK, CLAT, CLAT2, CLDEC, CLVSM, CMA1, CMA2, CMD1, CMD10, CMD11, CMD12, CMD2, CMD3, CMD4, CMD5, CMD6, CMD7, CMD8, CMD9, CMT1F, CMT2F, COF1, COR1, COR2, CRST, CSCH, CSCH2, CSCH3, CSINA1, CSINA2, CSINA3, CSIND, CSINF1, CSINF2, CSNUF, CSNVF, CSNWF, CTAMBF, CTHSF, CUB1, CUB2, CUS1, CUS2, CV25, CVB1, CVB2, CVD1, CVD2, CVDIG, CVM1, CVM2, CVS1, CVS2, CWB1, CWB2, CWS1, CWS2, CYA, CYB: footprint C0603 -> traction:C_0603_1608Metric
- CEXD, CLVC1: footprint C1206 -> traction:C_1206_3216Metric
- CLDE, CLVC2: footprint C1210 -> traction:C_1210_3225Metric
- CLVC3: footprint CAP-ALU-SMD-G-10x10.2 -> traction:CP_Elec_10x10.5
- CSB1, CSB2, CSB3, CSB3B, CSB4, CSB5, CSB6, CSB7, CSB8, CVBOS: footprint C0805 -> traction:C_0805_2012Metric
- DBAT, DCLR, DFLT1, DFLT2, DFO, ZLVS, ZSET: footprint SOD123 -> traction:D_SOD-123
- DCOSP, DSINP, QBAL, QLVN, TVSC1, TVSC2: footprint SOT23 -> traction:SOT-23-3
- DEXN, DEXP: footprint SOD128 -> traction:D_SOD-128
- DIGN, TVSM1, TVSM2: footprint SMA -> traction:D_SMA
- DREVC, DTVSC, DTVSC2, TVSEN, TVSEP: footprint SMC -> traction:D_SMC
- FEXN, FEXP: footprint 1812 -> traction:Fuse_1812_4532Metric
- FLVC: footprint 2410 -> traction:Bel_0680L_2410
- FMT1, FMT2: footprint F0603 -> traction:Fuse_0603_1608Metric
- FVBH, FVBL: footprint PTC2920 -> traction:Fuse_2920_7451Metric
- FVS1: footprint PTC1812 -> traction:Fuse_1812_4532Metric
- JICC: footprint HDR2x20-2.54 -> traction:Samtec_IPL1-120_2x20
- JLEM: footprint HDR2x5 -> traction:PinHeader_2x05_P2.00mm_Vertical
- JSWD: footprint HDR2x5-1.27 -> traction:PinHeader_2x05_P1.27mm_Vertical
- JVEH: footprint AMPSEAL23 -> traction:TE_770669-1
- LCAN1, LCAN2: footprint CMC1210 -> traction:TDK_ACT45B
- LCOR: footprint XAL4020 -> traction:L_Coilcraft_XAL4020-XXX
- LFC: footprint FB1206 -> traction:L_1206_3216Metric
- LSBC: footprint XAL4040 -> traction:L_Coilcraft_XAL4040-XXX
- LUB, LVB, LWB: footprint FB0805 -> traction:L_0805_2012Metric
- LVS1, LVS2, LVS3, LVS4: footprint FB0603 -> traction:L_0603_1608Metric
- QLVS: footprint SOT223 -> traction:SOT-223
- RAGT: footprint R0805 -> traction:R_0805_2012Metric
- RARB, RASCP, RBOOT, RCOS1, RCOS2, RCOSF1, RCOSF2, RCOSR1, RCOSR2, RCPD0, RCPD1, RCPD2, RCPD3, RCT1A, RCT1B, RCT2A, RCT2B, RDBG, RDRB, RENP1, REXA1, REXA2, REXA3, REXA4, REXB1, REXB2, REXB3, REXB4, REXM1, REXM2, REXM3, REXM4, RFCB, RFLTC, RFLTD, RFLTP1, RFLTP2, RFS1, RFS2, RFS3, RGPD, RHWP, RIGN1, RIGN2, RIGNS1, RIGNS2, RILK1, RILK2, RILK3, RILK4, RLAT1, RLAT2, RLDE1, RLDE2, RLVSD, RLVSG, RLVSM, RMRST, RMT1P, RMT1S, RMT2P, RMT2S, ROF1, ROF2, RQDM, RRDB, RRDYP1, RRDYP2, RSB1, RSB2, RSB3, RSB4, RSCH, RSDN, RSIN1, RSIN2, RSINF1, RSINF2, RSINR1, RSINR2, RSNUP, RSNVP, RSNWP, RTAMB, RTAMBP, RTHS, RTHSP, RTMR, RUB0, RUB1, RUB2, RUB3, RV5GP, RV5GS, RVB0, RVB1, RVB2, RVB3, RVD1A, RVD1B, RVD1C, RVD1D, RVD2A, RVD2B, RVD2C, RVD2D, RVM1, RVM2, RVM3, RVM4, RWB0, RWB1, RWB2, RWB3: footprint R0603 -> traction:R_0603_1608Metric
- RFS4, RSXN, RSXP: footprint R1206 -> traction:R_1206_3216Metric
- UAND1, UAND2: footprint SOT363 -> traction:SOT-363_SC-70-6
- UASCG, UOR1, UOR2: footprint SOT353 -> traction:SOT-353_SC-70-5
- UCAN1, UCAN2: footprint SOIC8 -> traction:SOIC-8_3.9x4.9mm_P1.27mm
- UEXD: footprint HTSSOP14-PWP -> traction:ALM2402-Q1_PWP0014H
- UEXF, UMT1, UMT2, UUB1, UUB2, UVB1, UVB2, UVD1, UVD2, UVMB1, UVMB2, UVOF, UWB1, UWB2: footprint SOT23-5 -> traction:SOT-23-5
- ULAT, ULAT2, USCH, USCH2, USCH3: footprint VSSOP8 -> traction:VSSOP-8_2.3x2mm_P0.5mm
- ULDOEX: footprint DPAK5 -> traction:TO-252-5_TabPin3
- UMCU: footprint MAPBGA289 -> traction:MAPBGA-289_14x14mm_Layout17x17_P0.8mm
- USBC: footprint HLQFP48 -> traction:FS26_HLQFP48
- USNSU, USNSV, USNSW: footprint OffBoard -> (none)
- Y1: footprint X3225 -> traction:Kyocera_CX3225GA_2Pad
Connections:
- net AGND: now also UEXD.14, UEXD.15 (PAD), UEXD.6
- net EXN1: now also UEXD.1 (IN1N)
- net EXN2: now also UEXD.5 (IN2N)
- net EXSD: now also UEXD.3 (SDN)
- net VEXD: now also UEXD.10 (VCCO2), UEXD.11, UEXD.12 (VCCO1)
- net VMID_REX: now also UEXD.2 (IN1P), UEXD.4 (IN2P)
- net VREX_N: now also UEXD.9 (OUT2)
- net VREX_P: now also UEXD.13 (OUT1)
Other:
- note added: "rev A.21 - 26 sections - 301 components"
- note removed: "rev A.20 - 26 sections - 301 components"
- moved on the sheet: CEXD, REXB1, REXB2, REXB3, REXB4, RSDN, UEXD
